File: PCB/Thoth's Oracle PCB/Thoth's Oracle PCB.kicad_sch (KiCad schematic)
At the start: 9 parts, among them J1 IO, J2 MCUDisplay, J3 Display, SW1 Orientation, SW2 Prev, SW3 Play/Pause, SW4 Next, SW5 RotaryEncoder_Switch

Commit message: Cleaned board
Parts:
- J3: footprint Connector_PinSocket_2.54mm:PinSocket_1x08_P2.54mm_Vertical -> Connector_PinSocket_2.54mm:PinSocket_1x08_P2.54mm_Horizontal
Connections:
- net +5V: now also J3.1 (Pin_1); no longer J3.8 (Pin_8)
- net GND: now also J3.2 (Pin_2); no longer J3.7 (Pin_7)
- net LED: now also J3.8 (Pin_8); no longer J3.1 (Pin_1)
- net P10: now also J3.6 (Pin_6); no longer J3.3 (Pin_3)
- net P11: now also J3.7 (Pin_7); no longer J3.2 (Pin_2)
- net P12: now also J3.4 (Pin_4); no longer J3.5 (Pin_5)
- net P13: now also J3.3 (Pin_3); no longer J3.6 (Pin_6)
- net P9: now also J3.5 (Pin_5); no longer J3.4 (Pin_4)
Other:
- moved on the sheet: J3
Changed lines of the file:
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@@
 	(wire
 		(pts
-			(xy 29.21 88.9) (xy 34.29 88.9)
+			(xy 22.86 88.9) (xy 34.29 88.9)
 		)
 		(stroke
@@
 	(wire
 		(pts
-			(xy 29.21 83.82) (xy 36.83 83.82)
+			(xy 22.86 83.82) (xy 36.83 83.82)
 		)
 		(stroke
@@
 	(wire
 		(pts
-			(xy 29.21 96.52) (xy 30.48 96.52)
+			(xy 22.86 96.52) (xy 30.48 96.52)
 		)
 		(stroke
@@
 	(wire
 		(pts
-			(xy 29.21 78.74) (xy 39.37 78.74)
+			(xy 22.86 78.74) (xy 39.37 78.74)
 		)
 		(stroke
@@
 	(wire
 		(pts
-			(xy 29.21 93.98) (xy 31.75 93.98)
+			(xy 22.86 93.98) (xy 31.75 93.98)
 		)
 		(stroke
@@
 	(wire
 		(pts
-			(xy 29.21 91.44) (xy 33.02 91.44)
+			(xy 22.86 91.44) (xy 33.02 91.44)
 		)
 		(stroke
@@
 	(wire
 		(pts
-			(xy 29.21 86.36) (xy 35.56 86.36)
-		)
-		(stroke
-			(width 0)
-			(type default)
-		)
-	)
-	(wire
-		(pts
-			(xy 29.21 81.28) (xy 38.1 81.28)
+			(xy 22.86 86.36) (xy 35.56 86.36)
+		)
+		(stroke
+			(width 0)
+			(type default)
+		)
+	)
+	(wire
+		(pts
+			(xy 22.86 81.28) (xy 38.1 81.28)
 		)
 		(stroke
@@
 	(symbol
 		(lib_id "Connector:Conn_01x08_Pin")
-		(at 24.13 86.36 0)
+		(at 27.94 88.9 180)
 		(unit 1)
 		(exclude_from_sim no)
@@
 		(fields_autoplaced yes)
 		(property "Reference" "J3"
-			(at 24.765 73.66 0)
-			(effects
-				(font
-					(size 1.27 1.27)
-				)
+			(at 29.21 86.3599 0)
+			(effects
+				(font
+					(size 1.27 1.27)
+				)
+				(justify right)
 			)
 		)
 		(property "Value" "Display"
-			(at 24.765 76.2 0)
-			(effects
-				(font
-					(size 1.27 1.27)
-				)
-			)
-		)
-		(property "Footprint" "Connector_PinSocket_2.54mm:PinSocket_1x08_P2.54mm_Vertical"
-			(at 24.13 86.36 0)
+			(at 29.21 88.8999 0)
+			(effects
+				(font
+					(size 1.27 1.27)
+				)
+				(justify right)
+			)
+		)
+		(property "Footprint" "Connector_PinSocket_2.54mm:PinSocket_1x08_P2.54mm_Horizontal"
+			(at 27.94 88.9 0)
 			(effects
 				(font
@@
 		)
 		(property "Datasheet" "~"
-			(at 24.13 86.36 0)
+			(at 27.94 88.9 0)
 			(effects
 				(font
@@
 		)
 		(property "Description" "Generic connector, single row, 01x08, script generated"
-			(at 24.13 86.36 0)
-			(effects
-				(font
+			(at 27.94 88.9 0)
+			(effects
+				(font

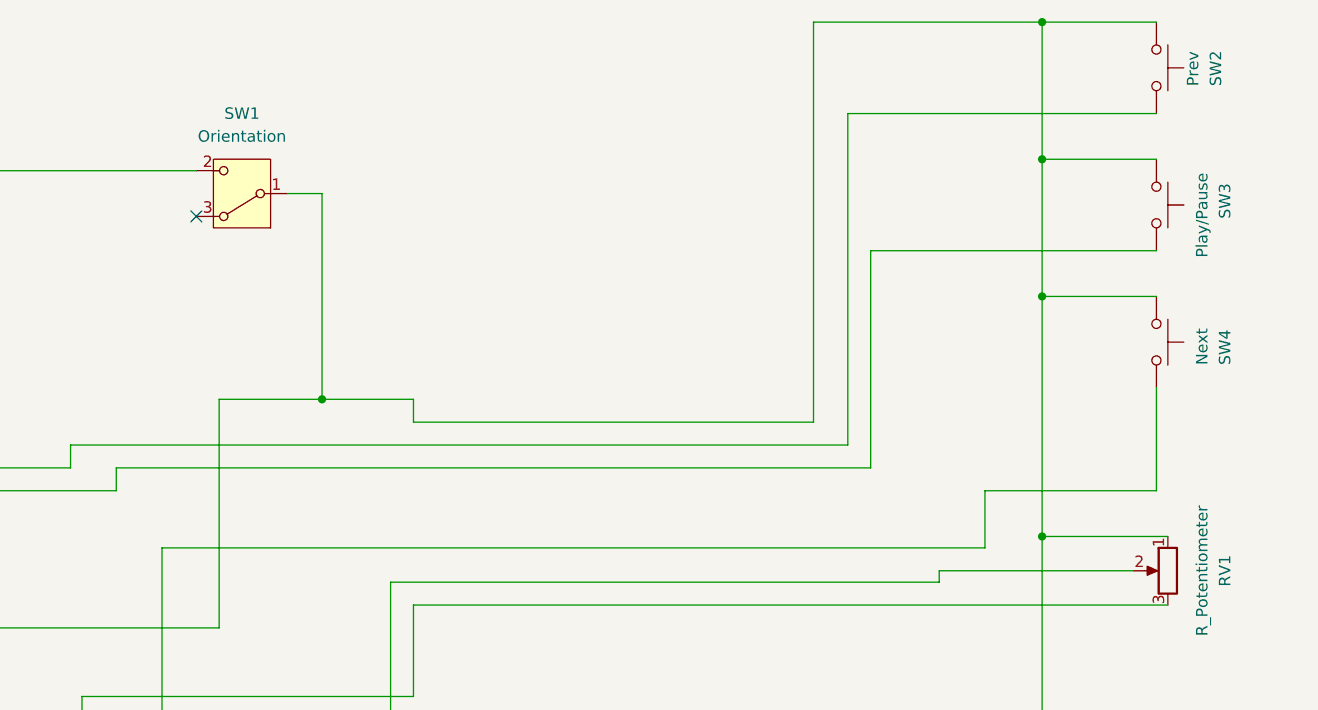
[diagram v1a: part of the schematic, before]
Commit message: Separated hotswap sockets with modified footprints so they don't overlap. Typo in assembly
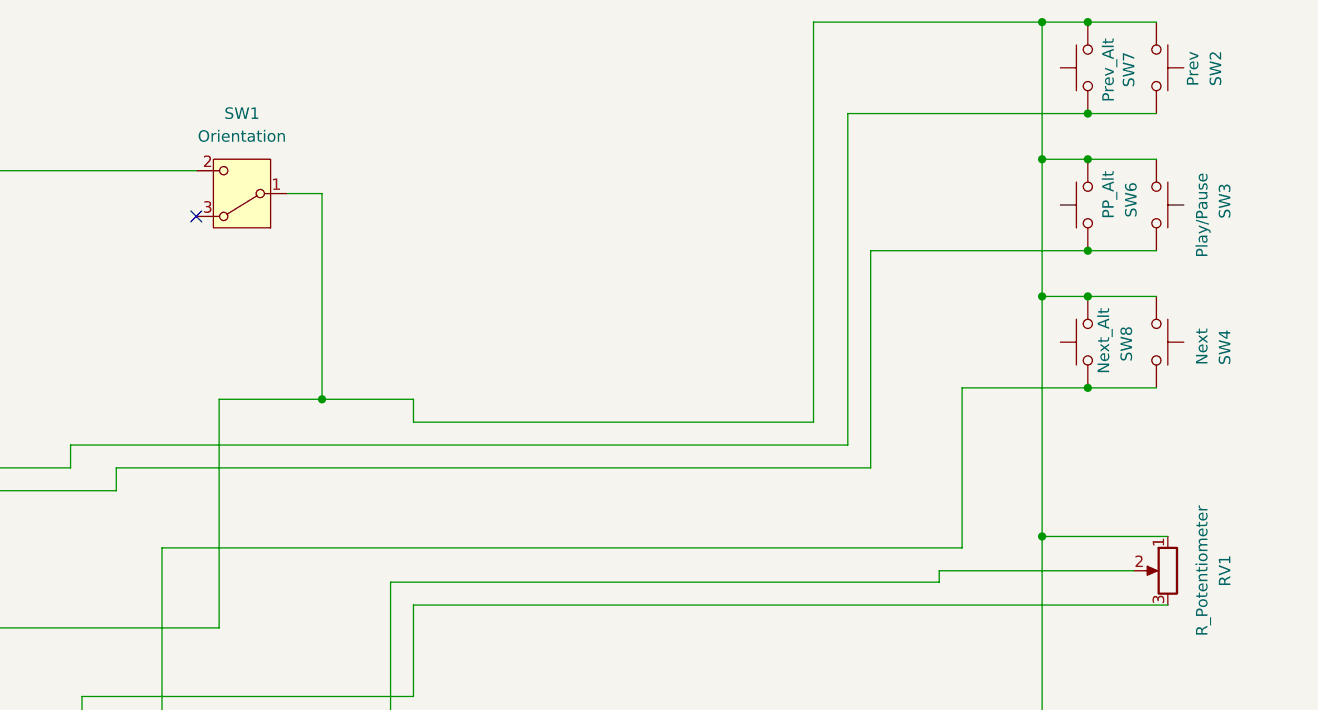
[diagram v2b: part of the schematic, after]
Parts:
- added SW6: PP_Alt, keyswitches:Kailh_socket_PG1350_modified, symbol Switch:SW_Push
- added SW7: Prev_Alt, keyswitches:Kailh_socket_PG1350_modified, symbol Switch:SW_Push
- added SW8: Next_Alt, keyswitches:Kailh_socket_PG1350_modified, symbol Switch:SW_Push
- SW2, SW3, SW4: footprint keyswitches:Kailh_socket_MX_PG1350 -> keyswitches:Kailh_socket_MX_modified
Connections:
- net GND: now also SW6.2, SW7.2, SW8.2
- net P6: now also SW8.1
- net P7: now also SW7.1
- net P8: now also SW6.1

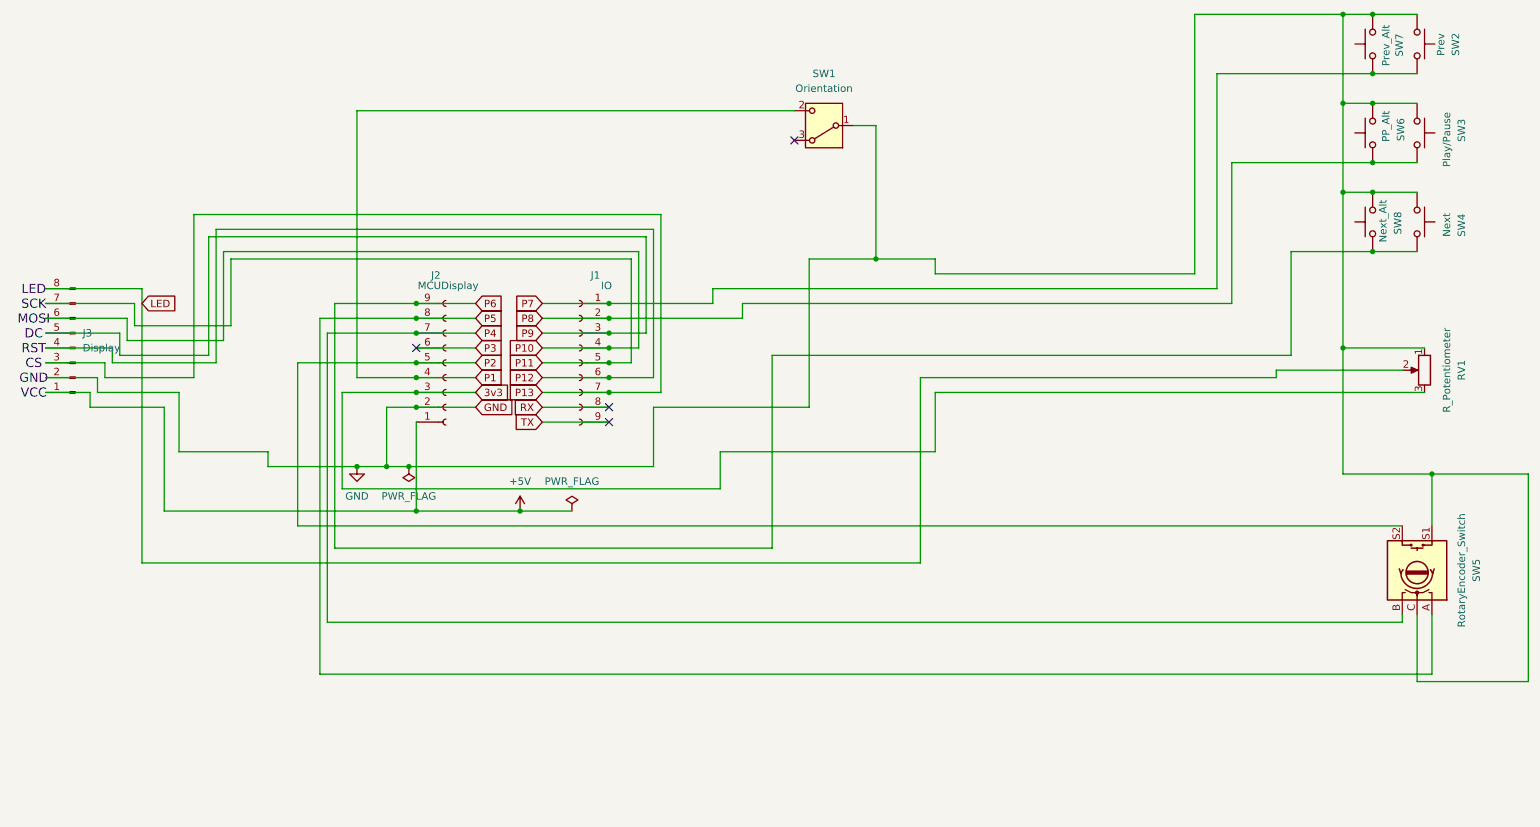
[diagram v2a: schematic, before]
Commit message: Working on gif capabilites with 8-bit parallel display instead of SPI
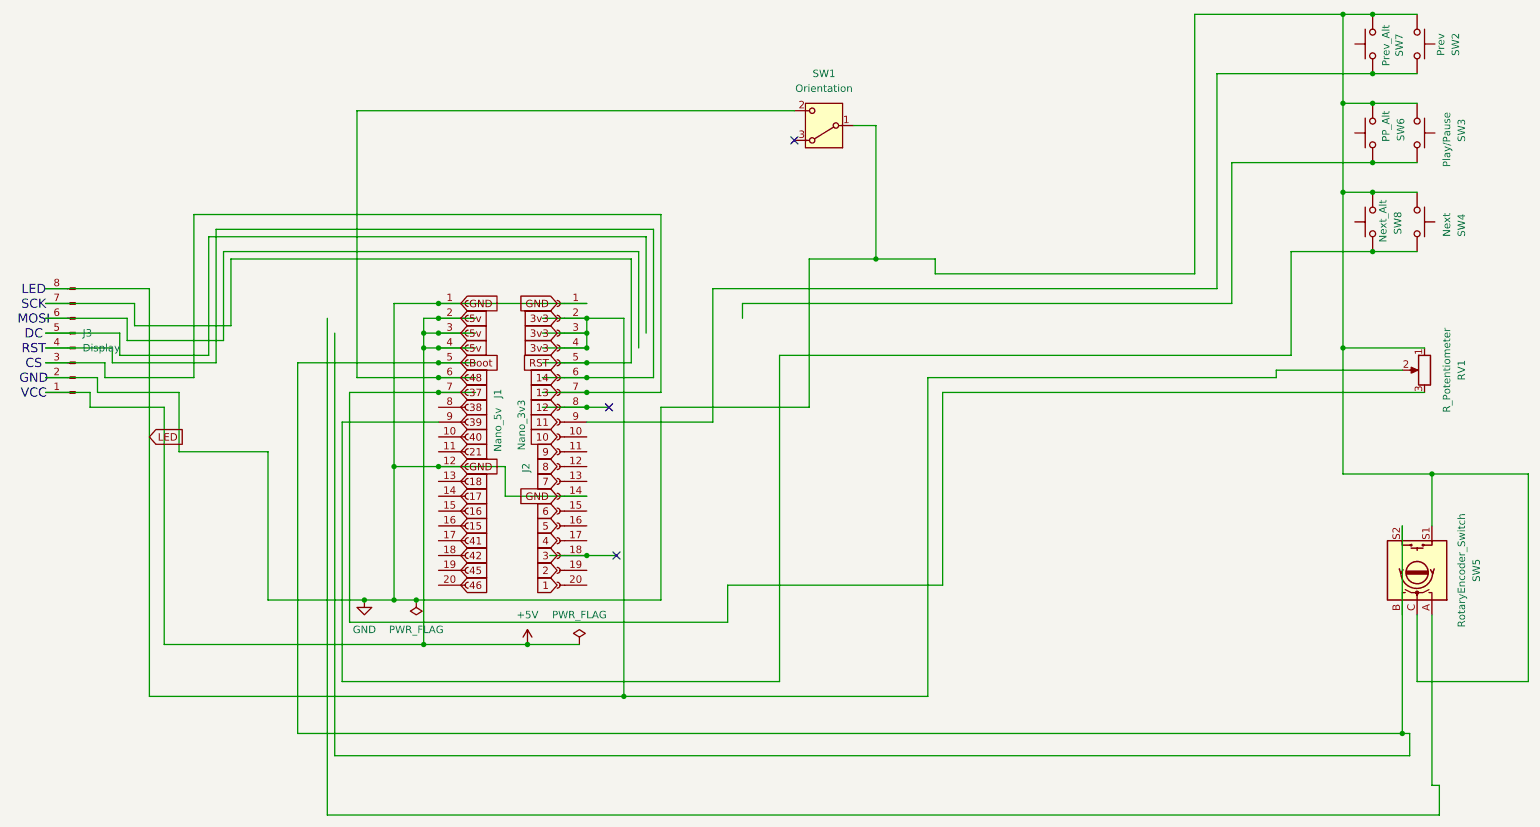
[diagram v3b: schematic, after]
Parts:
- removed J1: IO, Connector_PinSocket_2.54mm:PinSocket_1x09_P2.54mm_Vertical, symbol Connector:Conn_01x09_Socket
- removed J2: MCUDisplay, Connector_PinSocket_2.54mm:PinSocket_1x09_P2.54mm_Vertical, symbol Connector:Conn_01x09_Socket
- added J1: Nano_5v, Connector_PinSocket_2.54mm:PinSocket_1x20_P2.54mm_Vertical, symbol Connector:Conn_01x20_Socket
- added J2: Nano_3v3, Connector_PinSocket_2.54mm:PinSocket_1x20_P2.54mm_Vertical, symbol Connector:Conn_01x20_Socket
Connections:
- net LED is gone; now on net 3v3: J3.8 (Pin_8), RV1.2
- net +5V: now also J1.2 (Pin_2), J1.3 (Pin_3), J1.4 (Pin_4)
- net 3v3: now also J2.2 (Pin_2), J2.3 (Pin_3), J2.4 (Pin_4); no longer RV1.3
- net GND: now also J1.1 (Pin_1), J1.12 (Pin_12), J2.1 (Pin_1), J2.14 (Pin_14)
- net P1 renamed 48
- net 48: now also J1.6 (Pin_6)
- net P10: no longer names the net of J3.6 (Pin_6)
- net P11 renamed RST
- net RST: now also J2.5 (Pin_5)
- net P12 renamed 14
- net 14: now also J2.6 (Pin_6)
- net P13 renamed 13
- net 13: now also J2.7 (Pin_7)
- net P2 renamed Boot
- net Boot: now also J1.5 (Pin_5)
- net P4: no longer names the net of SW5.B
- net P5: no longer names the net of SW5.A
- net P6: no longer names the net of SW4.1, SW8.1
- net P6: now also J1.9 (Pin_9)
- net P7: no longer names the net of SW2.1, SW7.1
- net P7: now also J2.9 (Pin_9)
- net P8: no longer names the net of SW3.1, SW6.1
- net P9: no longer names the net of J3.5 (Pin_5)
- new net 12: J2.8 (Pin_8)
- new net 3: J2.18 (Pin_18)
- new net 37: J1.7 (Pin_7), RV1.3
- no-connect marks 4 -> 3
